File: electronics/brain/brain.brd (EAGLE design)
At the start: 59.7 x 53.3 mm, 7 parts

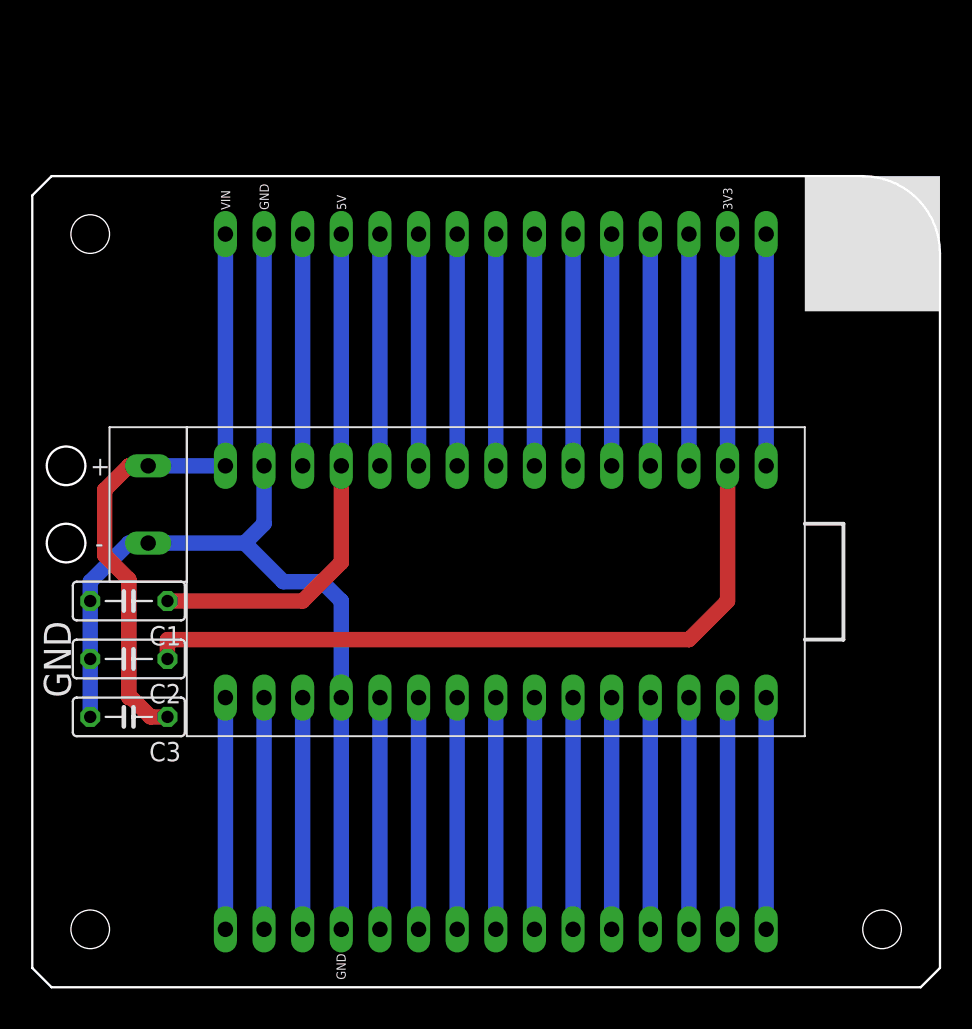
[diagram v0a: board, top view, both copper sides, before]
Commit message: Fleshed out pin mapping. Routed new brain board.
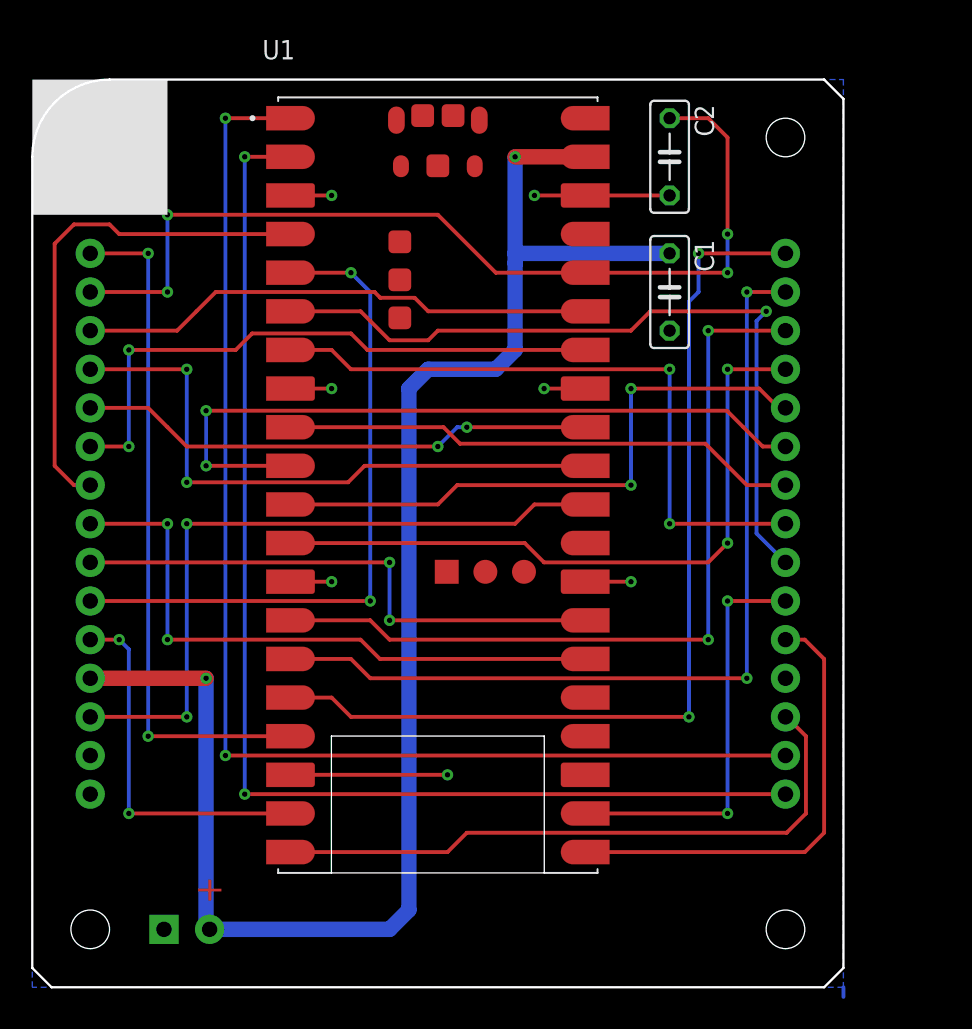
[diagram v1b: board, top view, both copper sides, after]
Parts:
- removed C3: (no value), rcl:C050-025X075
- removed U$1: ARDUINO-NANO-V3, RC Car:ARDUINO-NANO-V3
- removed U$2: ARDUINO-NANO-JUMPER-1, RC Car:ARDUINO-NANO-JUMPER-1
- removed U$3: POWER-IN, RC Car:POWER-IN
- removed U$5: ARDUINO-NANO-JUMPER-2, RC Car:ARDUINO-NANO-JUMPER-2
- added U$4: RC_FORM_FACTOR, rc_car:RC_FORM_FACTOR
- added U$6: LIPO_BATTERY, GIX:JST_PH
- added U1: SC0918, SC0918:MODULE_SC0918
- moved C2 48.5 mm to (41.9, 54.6), turned to 270 degrees
- moved C1 41.0 mm to (41.9, 45.7), turned to 270 degrees
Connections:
- removed net +5V: C1.1, U$1.5V, U$5.5V
- removed net A00: U$1.A00, U$5.A0
- removed net A01: U$1.A01, U$5.A1
- removed net A02: U$1.A02, U$5.A2
- removed net A03: U$1.A03, U$5.A3
- removed net A04: U$1.A04, U$5.A4
- removed net A05: U$1.A05, U$5.A5
- removed net A06: U$1.A06, U$5.A6
- removed net A07: U$1.A07, U$5.A7
- removed net D02: U$1.D02, U$2.D2
- removed net D03: U$1.D03, U$2.D3
- removed net D04: U$1.D04, U$2.D4
- removed net D05: U$1.D05, U$2.D5
- removed net D06: U$1.D06, U$2.D6
- removed net D07: U$1.D07, U$2.D7
- removed net D08: U$1.D08, U$2.D8
- removed net D09: U$1.D09, U$2.D9
- removed net D10: U$1.D10, U$2.D10
- removed net D11: U$1.D11, U$2.D11
- removed net D12: U$1.D12, U$2.D12
- removed net D13: U$1.D13, U$5.D13
- removed net REF: U$1.REF, U$5.REF
- removed net RST: U$1.RST, U$1.RST@1, U$2.RST, U$5.RST
- removed net RX0: U$1.RX0, U$2.RX0
- removed net TX1: U$1.TX1, U$2.TX1
- removed net V+: C3.1, U$1.VIN, U$3.POS, U$5.VIN
- new net 1: U$4.1, U1.17
- new net 10: U$4.10, U1.5
- new net 11: U$4.11, U1.19
- new net 13: U$4.13, U1.30
- new net 15: U$4.15
- new net 16: U$4.16, U1.2
- new net 17: U$4.17, U1.1
- new net 18: U$4.18, U1.20
- new net 20: U$4.20, U1.21
- new net 21: U$4.21, U1.22
- new net 22: U$4.22, U1.6
- new net 23: U$4.23, U1.7
- new net 24: U$4.24, U1.9
- new net 25: U$4.25, U1.10
- new net 26: U$4.26, U1.11
- new net 27: U$4.27, U1.12
- new net 28: U$4.28, U1.14
- new net 29: U$4.29, U1.15
- new net 3: U$4.3, U1.35
- new net 30: U$4.30, U1.16
- new net 4: U$4.4, U1.31
- new net 5: U$4.5, U1.32
- new net 6: U$4.6, U1.34
- new net 7: U$4.7, U1.4
- new net 8: U$4.8, U1.26
- new net 9: U$4.9, U1.27
- new net AGND: U1.33
- new net TP1_GND: U1.TP1
- new net USB_SHIELD: U1.A, U1.B, U1.C, U1.D
- new net VBUS: U1.40
- new net VCC: C1.1, U$4.12, U$6.POS, U1.39
- net +3V3: now also U$4.2, U1.36; no longer U$1.3V3, U$5.3V3
- net GND: now also U$4.14, U$4.19, U$6.GND, U1.13, U1.18, U1.23, U1.28, U1.3, U1.38, U1.8, U1.F; no longer C3.2, U$1.GND, U$1.GND@1, U$2.GND, U$3.NEG, U$5.GND
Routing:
- net VCC: track 0.00 -> 107.8 mm, vias 0 -> 2
- net 17: track 0.00 -> 83.0 mm, vias 0 -> 2
- net 16: track 0.00 -> 80.5 mm, vias 0 -> 2
- net 30: track 0.00 -> 63.2 mm, vias 0 -> 2
- net 29: track 0.00 -> 58.5 mm, vias 0 -> 2
- net 28: track 0.00 -> 53.4 mm, vias 0 -> 2
- net 22: track 0.00 -> 50.4 mm, vias 0 -> 1
- net 25: track 0.00 -> 48.2 mm, vias 0 -> 2
- net 13: track 0.00 -> 45.8 mm, vias 0 -> 2
- net 27: track 0.00 -> 45.0 mm, vias 0 -> 2
- net 1: track 0.00 -> 44.9 mm, vias 0 -> 2
- net 10: track 0.00 -> 44.5 mm, vias 0 -> 2
- net 23: track 0.00 -> 43.2 mm, vias 0 -> 2
- net 18: track 0.00 -> 41.9 mm
- net V+: track 41.2 -> 0.00 mm
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- added copper zone on layer 16, net GND
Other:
- board size 59.7 x 53.3 mm -> 53.3 x 59.7 mm
- board text removed: "+"
- board text removed: "-"
- board text removed: "3V3"
- board text removed: "5V"
- board text removed: "GND"
- board text removed: "RC CARS BRAIN BOARD NANO EDITION"
- board text removed: "VIN"
